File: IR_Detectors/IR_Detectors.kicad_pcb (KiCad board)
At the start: 2 copper layers, 19 parts, among them Q1 LTR-3208E, Q2 2N7000, U1 LM6144xIx, U2 MCP6294

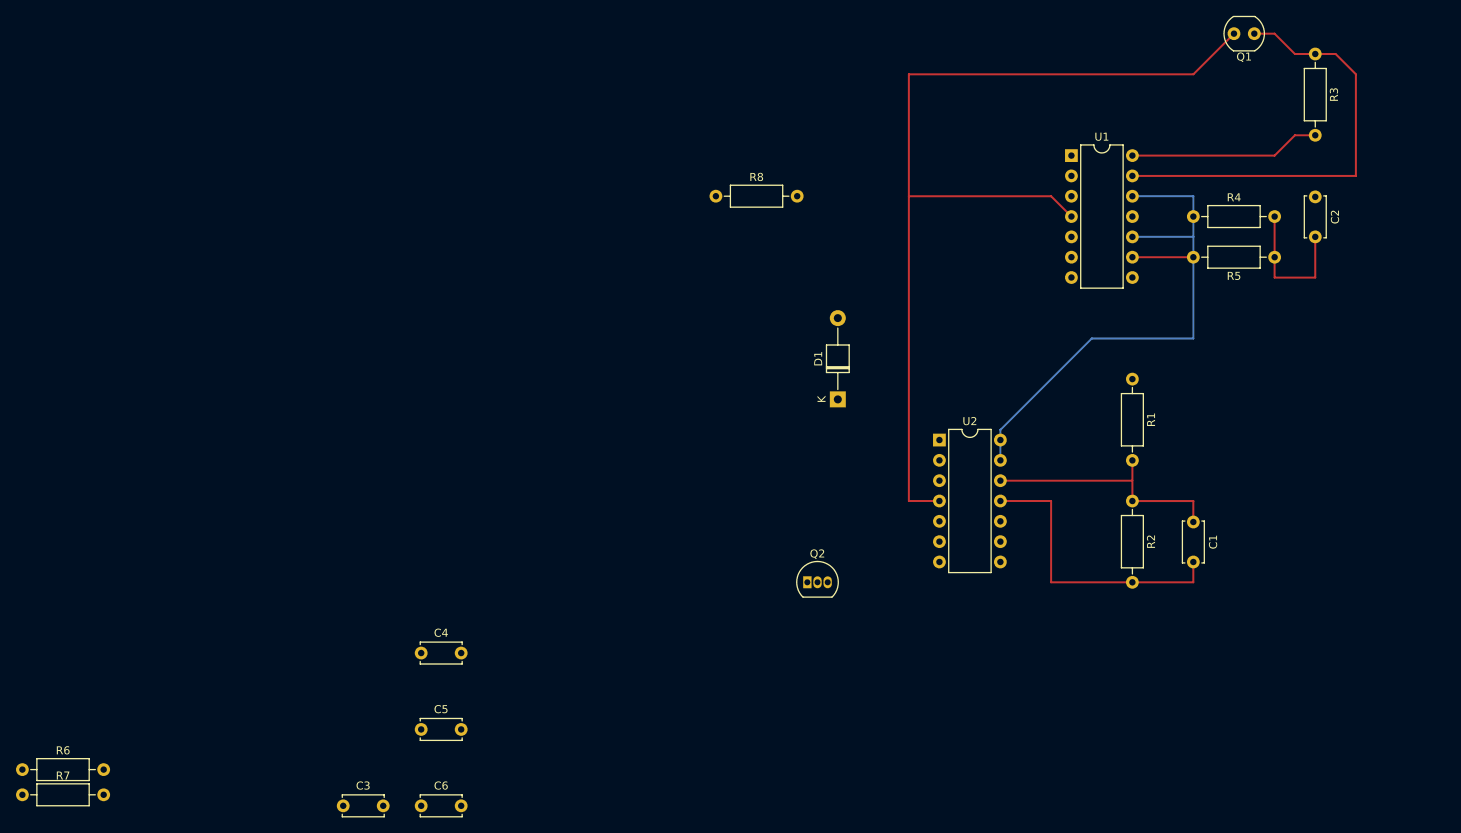
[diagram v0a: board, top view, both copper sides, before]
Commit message: single IR detector design
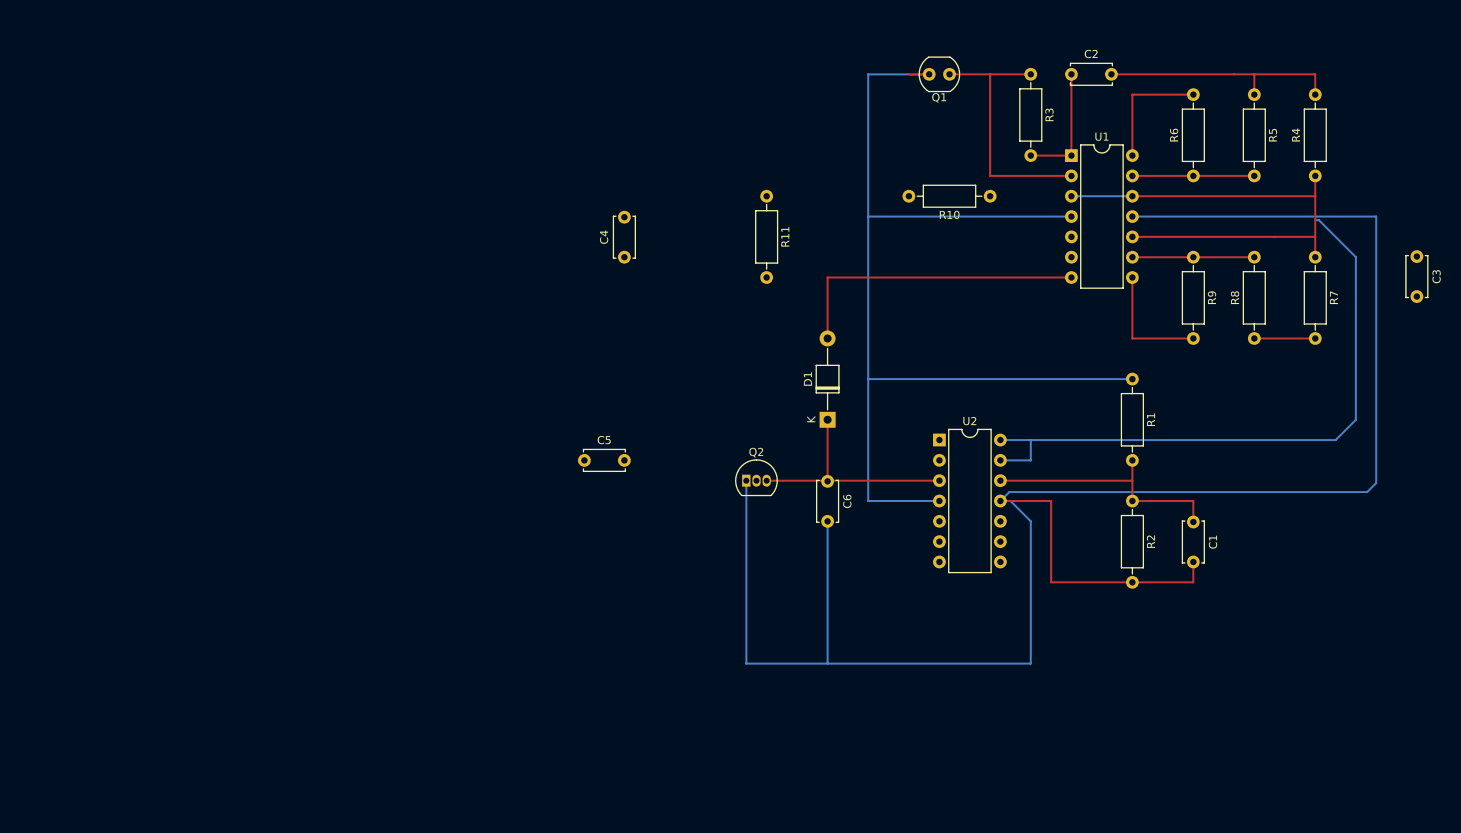
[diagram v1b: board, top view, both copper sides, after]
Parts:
- removed the C5 at (99.1, 153.0)
- added C4: 10nF, Capacitor_THT:C_Disc_D5.0mm_W2.5mm_P5.00mm, F.Cu at (124.5, 94.0)
- added R10: 10k, Resistor_THT:R_Axial_DIN0207_L6.3mm_D2.5mm_P10.16mm_Horizontal, F.Cu at (170.2, 86.4)
- added R8: 10k, Resistor_THT:R_Axial_DIN0207_L6.3mm_D2.5mm_P10.16mm_Horizontal, F.Cu at (203.2, 104.1)
- added R9: 100k, Resistor_THT:R_Axial_DIN0207_L6.3mm_D2.5mm_P10.16mm_Horizontal, F.Cu at (195.6, 94.0)
- R3: value 680 -> 4.7k
- R5: value 2.2k -> 100
- moved R7 175.0 mm to (210.8, 94.0), turned to -90 degrees
- moved R6 164.1 mm to (195.6, 83.8), turned to 90 degrees
- moved C3 150.7 mm to (223.5, 93.9), turned to -90 degrees
- moved C6 65.0 mm to (149.9, 122.0), turned to -90 degrees
- moved Q1 38.4 mm to (165.1, 71.1)
- moved R3 35.7 mm to (175.3, 71.1)
- moved C2 34.1 mm to (180.3, 71.1), turned to 0 degrees
- moved C5 31.6 mm to (119.5, 119.4)
- moved R5 20.5 mm to (203.2, 73.7), turned to -90 degrees
- moved R4 16.1 mm to (210.8, 83.8), turned to 90 degrees
- moved Q2 14.8 mm to (139.7, 121.9)
- moved R11 6.34 mm to (142.2, 86.4), turned to -90 degrees
- moved D1 2.85 mm to (149.9, 114.3)
- renumbered C4 to C5, R8 to R11
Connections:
- R11 pad 1: unconnected-(R8-Pad1) -> Net-(C4-Pad2)
- R5 pad 2: Net-(U1C--) -> Net-(U1D--)
- R6 pad 1: Net-(U1C--) -> Net-(U1D--)
- U1 pad 1: (no net) -> Net-(C2-Pad1)
- U1 pad 13: Net-(Q1-E) -> Net-(U1D--)
- U1 pad 14: Net-(C2-Pad1) -> Net-(C3-Pad1)
- U1 pad 2: (no net) -> Net-(Q1-E)
- U1 pad 3: (no net) -> /+2.5V
- U1 pad 8: Net-(C3-Pad1) -> Net-(C4-Pad1)
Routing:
- net GND: track 36.8 -> 251.2 mm
- net /+2.5V: track 65.7 -> 142.7 mm
- net Net-(D1-A): track 0.00 -> 38.1 mm
- net Net-(D1-K): track 0.00 -> 29.4 mm
- net Net-(Q1-E): track 55.4 -> 33.0 mm
- net Net-(C4-Pad1): track 0.00 -> 15.2 mm
- net Net-(C3-Pad1): track 0.00 -> 15.2 mm
- net Net-(U1D--): track 0.00 -> 15.2 mm
- net Net-(C2-Pad2): track 17.8 -> 30.6 mm
- net +5V: track 121.3 -> 130.8 mm
- net Net-(C2-Pad1): track 23.9 -> 15.2 mm
- net Net-(C3-Pad2): track 0.00 -> 7.62 mm
- net Net-(U1C--): track 7.62 -> 15.2 mm
